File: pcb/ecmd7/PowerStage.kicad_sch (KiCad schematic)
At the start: 36 parts, among them Q1 IRFS3806, Q2 IRFS3806, Q3 IRFS3806, Q4 IRFS3806, Q5 IRFS3806, Q6 IRFS3806, U1 TMC6200-TA

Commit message: WIP: Add supply
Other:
- moved on the sheet: Q2, Q4, Q6, R2, R4, R7
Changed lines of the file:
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@@
 	(wire
 		(pts
+			(xy 290.83 171.45) (xy 300.99 171.45)
+		)
+		(stroke
+			(width 0)
+			(type default)
+		)
+	)
+	(wire
+		(pts
 			(xy 137.16 54.61) (xy 137.16 57.15)
 		)
@@
 	(wire
 		(pts
-			(xy 308.61 72.39) (xy 308.61 76.2)
+			(xy 308.61 73.66) (xy 308.61 76.2)
 		)
 		(stroke
@@
 	(wire
 		(pts
-			(xy 308.61 113.03) (xy 308.61 114.3)
+			(xy 308.61 113.03) (xy 308.61 115.57)
 		)
 		(stroke
@@
 	(wire
 		(pts
-			(xy 251.46 170.18) (xy 283.21 170.18)
+			(xy 251.46 171.45) (xy 283.21 171.45)
 		)
 		(stroke
@@
 	(wire
 		(pts
-			(xy 290.83 67.31) (xy 300.99 67.31)
+			(xy 290.83 68.58) (xy 300.99 68.58)
 		)
 		(stroke
@@
 	(wire
 		(pts
-			(xy 256.54 67.31) (xy 283.21 67.31)
+			(xy 256.54 68.58) (xy 283.21 68.58)
 		)
 		(stroke
@@
 	(wire
 		(pts
+			(xy 290.83 120.65) (xy 300.99 120.65)
+		)
+		(stroke
+			(width 0)
+			(type default)
+		)
+	)
+	(wire
+		(pts
 			(xy 256.54 163.83) (xy 308.61 163.83)
 		)
@@
 	(wire
 		(pts
-			(xy 256.54 67.31) (xy 256.54 102.87)
+			(xy 256.54 68.58) (xy 256.54 102.87)
 		)
 		(stroke
@@
 	(wire
 		(pts
-			(xy 251.46 133.35) (xy 251.46 170.18)
+			(xy 251.46 133.35) (xy 251.46 171.45)
 		)
 		(stroke
@@
 	(wire
 		(pts
-			(xy 290.83 119.38) (xy 300.99 119.38)
+			(xy 308.61 125.73) (xy 308.61 128.27)
 		)
 		(stroke
@@
 	(wire
 		(pts
-			(xy 308.61 124.46) (xy 308.61 128.27)
-		)
-		(stroke
-			(width 0)
-			(type default)
-		)
-	)
-	(wire
-		(pts
-			(xy 308.61 163.83) (xy 308.61 165.1)
+			(xy 308.61 163.83) (xy 308.61 166.37)
 		)
 		(stroke
@@
 	(wire
 		(pts
-			(xy 290.83 170.18) (xy 300.99 170.18)
-		)
-		(stroke
-			(width 0)
-			(type default)
-		)
-	)
-	(wire
-		(pts
 			(xy 219.71 92.71) (xy 237.49 92.71)
 		)
@@
 	(wire
 		(pts
-			(xy 265.43 119.38) (xy 265.43 118.11)
+			(xy 265.43 120.65) (xy 265.43 118.11)
 		)
 		(stroke
@@
 	(wire
 		(pts
-			(xy 265.43 119.38) (xy 283.21 119.38)
+			(xy 265.43 120.65) (xy 283.21 120.65)
 		)
 		(stroke
@@
 	(wire
 		(pts
-			(xy 308.61 175.26) (xy 308.61 179.07)
+			(xy 308.61 176.53) (xy 308.61 179.07)
 		)
 		(stroke
@@
 	(wire
 		(pts
-			(xy 308.61 60.96) (xy 308.61 62.23)
+			(xy 308.61 60.96) (xy 308.61 63.5)
 		)
 		(stroke
@@
 	(symbol
 		(lib_id "Device:R")
-		(at 287.02 67.31 90)
+		(at 287.02 68.58 90)
 		(unit 1)
 		(exclude_from_sim no)
@@
 		(dnp no)
 		(property "Reference" "R2"
-			(at 285.496 65.024 90)
+			(at 285.496 66.294 90)
 			(effects
 				(font
@@
 		)
 		(property "Value" "0.47"
-			(at 286.512 69.596 90)
+			(at 286.512 70.866 90)
 			(effects
 				(font
@@
 		)
 		(property "Footprint" "Resistor_SMD:R_0805_2012Metric"
-			(at 287.02 69.088 90)
+			(at 287.02 70.358 90)
 			(effects
 				(font
@@
 		)
 		(property "Datasheet" "~"
-			(at 287.02 67.31 0)
+			(at 287.02 68.58 0)
 			(effects
 				(font
@@
 		)
 		(property "Description" "Resistor"
-			(at 287.02 67.31 0)
+			(at 287.02 68.58 0)
 			(effects
 				(font
@@
 	(symbol
 		(lib_id "Transistor_FET:IRFS4115")
-		(at 306.07 67.31 0)
+		(at 306.07 68.58 0)
 		(unit 1)
 		(exclude_from_sim no)
@@
 		(fields_autoplaced yes)
 		(property "Reference" "Q2"
-			(at 312.42 66.0399 0)
+			(at 312.42 67.3099 0)
 			(effects
 				(font
@@
 		)
 		(property "Value" "IRFS3806"
-			(at 312.42 68.5799 0)
+			(at 312.42 69.8499 0)
 			(effects
 				(font
@@
 		)
 		(property "Footprint" "Package_TO_SOT_SMD:TO-263-2"
-			(at 311.15 69.215 0)
+			(at 311.15 70.485 0)
 			(effects
 				(font
@@
 		)
 		(property "Datasheet" "https://www.infineon.com/assets/row/public/documents/24/49/infineon-irfs3806-datasheet-en.pdf"
-			(at 311.15 71.12 0)
+			(at 311.15 72.39 0)
 			(effects
 				(font
@@
 		)
 		(property "Description" "43A Id, 60V Vds, 12.6mOhm Rds, N-Channel HEXFET Power MOSFET, D2PAK"
-			(at 306.07 67.31 0)
+			(at 306.07 68.58 0)
 			(effects
 				(font
@@
 	(symbol
 		(lib_id "Device:R")
-		(at 287.02 170.18 90)
+		(at 287.02 171.45 90)
 		(unit 1)
 		(exclude_from_sim no)
@@
 		(dnp no)
 		(property "Reference" "R7"
-			(at 285.496 167.894 90)
+			(at 285.496 169.164 90)
 			(effects
 				(font
@@
 		)
 		(property "Value" "0.47"
-			(at 286.512 172.466 90)
+			(at 286.512 173.736 90)
 			(effects
 				(font
@@
 		)
 		(property "Footprint" "Resistor_SMD:R_0805_2012Metric"
-			(at 287.02 171.958 90)
+			(at 287.02 173.228 90)
 			(effects
 				(font
@@
 		)
 		(property "Datasheet" "~"
-			(at 287.02 170.18 0)
+			(at 287.02 171.45 0)
 			(effects
 				(font
@@
 		)
 		(property "Description" "Resistor"
-			(at 287.02 170.18 0)
+			(at 287.02 171.45 0)
 			(effects
 				(font
@@
 	(symbol
 		(lib_id "Transistor_FET:IRFS4115")
-		(at 306.07 170.18 0)
+		(at 306.07 171.45 0)
 		(unit 1)
 		(exclude_from_sim no)
@@
 		(fields_autoplaced yes)
 		(property "Reference" "Q6"
-			(at 312.42 168.9099 0)
+			(at 312.42 170.1799 0)
 			(effects
 				(font
@@
 		)
 		(property "Value" "IRFS3806"
-			(at 312.42 171.4499 0)
+			(at 312.42 172.7199 0)
 			(effects
 				(font
@@
 		)
 		(property "Footprint" "Package_TO_SOT_SMD:TO-263-2"
-			(at 311.15 172.085 0)
+			(at 311.15 173.355 0)
 			(effects
 				(font
@@
 		)
 		(property "Datasheet" "https://www.infineon.com/assets/row/public/documents/24/49/infineon-irfs3806-datasheet-en.pdf"
-			(at 311.15 173.99 0)
+			(at 311.15 175.26 0)
 			(effects
 				(font
@@
 		)
 		(property "Description" "43A Id, 60V Vds, 12.6mOhm Rds, N-Channel HEXFET Power MOSFET, D2PAK"
-			(at 306.07 170.18 0)
+			(at 306.07 171.45 0)
 			(effects
 				(font
@@
 	(symbol
 		(lib_id "Transistor_FET:IRFS4115")
-		(at 306.07 119.38 0)
+		(at 306.07 120.65 0)
 		(unit 1)
 		(exclude_from_sim no)
@@
 		(fields_autoplaced yes)
 		(property "Reference" "Q4"
-			(at 312.42 118.1099 0)
+			(at 312.42 119.3799 0)
 			(effects
 				(font
@@
 		)
 		(property "Value" "IRFS3806"
-			(at 312.42 120.6499 0)
+			(at 312.42 121.9199 0)
 			(effects
 				(font
@@
 		)
 		(property "Footprint" "Package_TO_SOT_SMD:TO-263-2"
-			(at 311.15 121.285 0)
+			(at 311.15 122.555 0)
 			(effects
 				(font
@@
 		)
 		(property "Datasheet" "https://www.infineon.com/assets/row/public/documents/24/49/infineon-irfs3806-datasheet-en.pdf"
-			(at 311.15 123.19 0)
+			(at 311.15 124.46 0)
 			(effects
 				(font
@@
 		)
 		(property "Description" "43A Id, 60V Vds, 12.6mOhm Rds, N-Channel HEXFET Power MOSFET, D2PAK"
-			(at 306.07 119.38 0)
+			(at 306.07 120.65 0)
 			(effects
 				(font
@@
 	(symbol
 		(lib_id "Device:R")
-		(at 287.02 119.38 90)
+		(at 287.02 120.65 90)
 		(unit 1)
 		(exclude_from_sim no)
@@
 		(dnp no)
 		(property "Reference" "R4"
-			(at 285.496 117.094 90)
+			(at 285.496 118.364 90)
 			(effects
 				(font
@@
 		)
 		(property "Value" "0.47"
-			(at 286.512 121.666 90)
+			(at 286.512 122.936 90)
 			(effects
 				(font
@@
 		)
 		(property "Footprint" "Resistor_SMD:R_0805_2012Metric"
-			(at 287.02 121.158 90)
+			(at 287.02 122.428 90)
 			(effects
 				(font
@@
 		)
 		(property "Datasheet" "~"
-			(at 287.02 119.38 0)
+			(at 287.02 120.65 0)
 			(effects
 				(font
@@
 		)
 		(property "Description" "Resistor"
-			(at 287.02 119.38 0)
+			(at 287.02 120.65 0)
 			(effects
 				(font

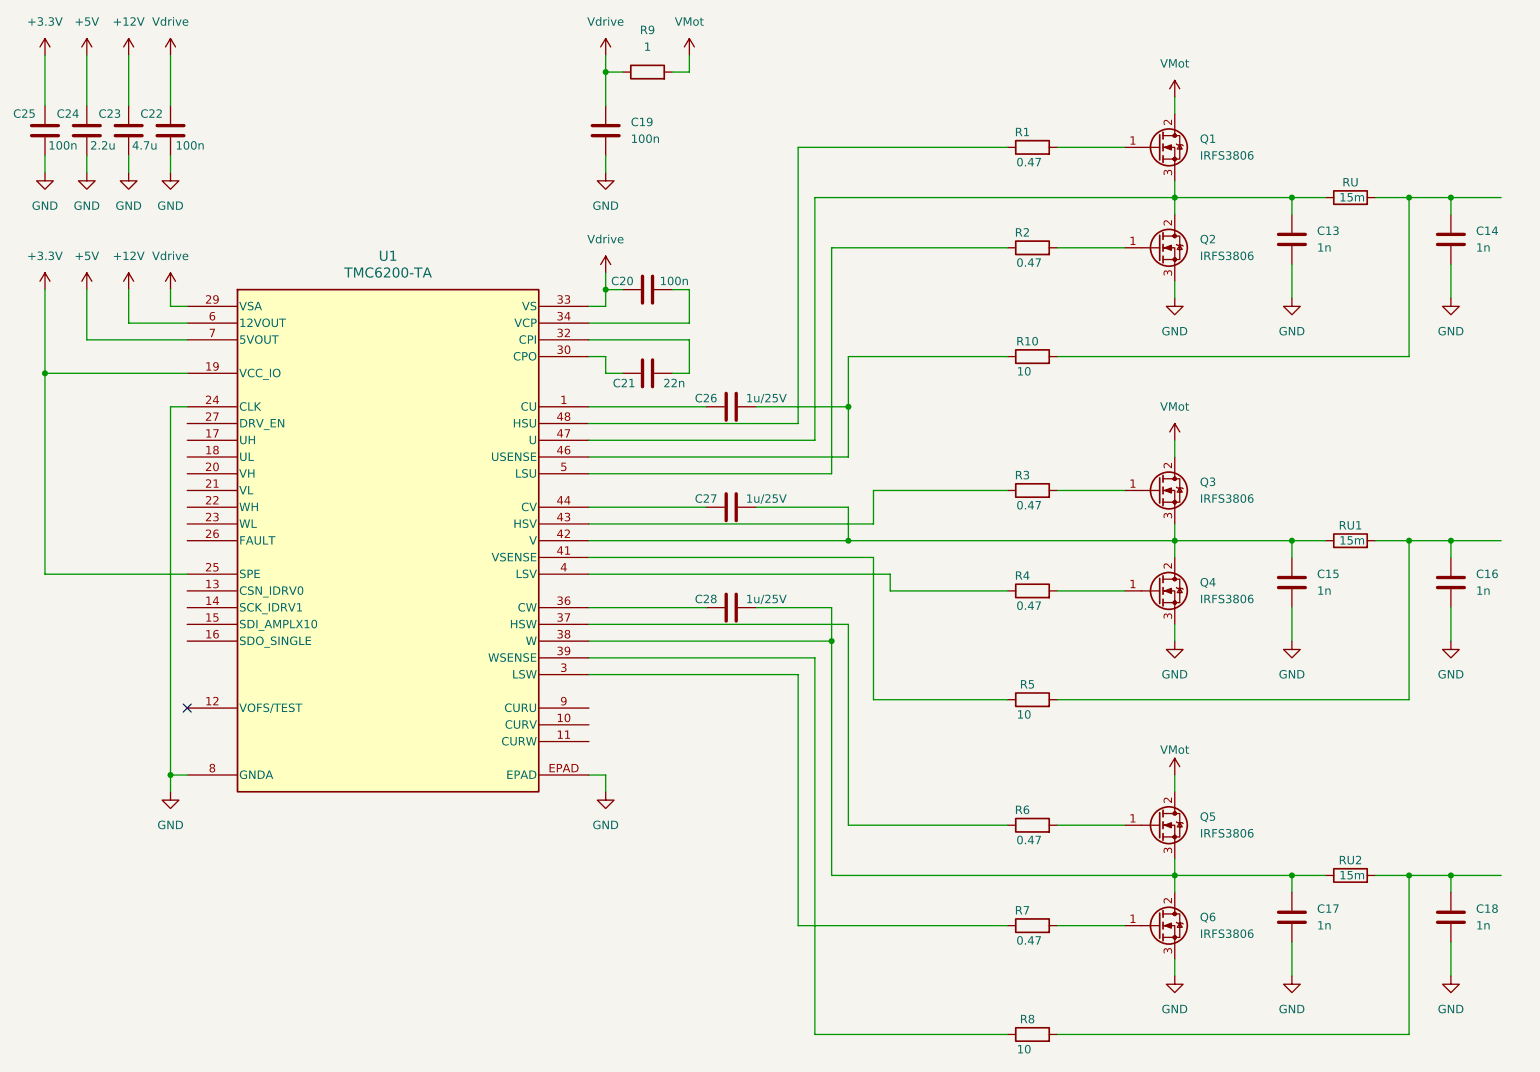
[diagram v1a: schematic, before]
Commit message: WIP: Add ADC inputs
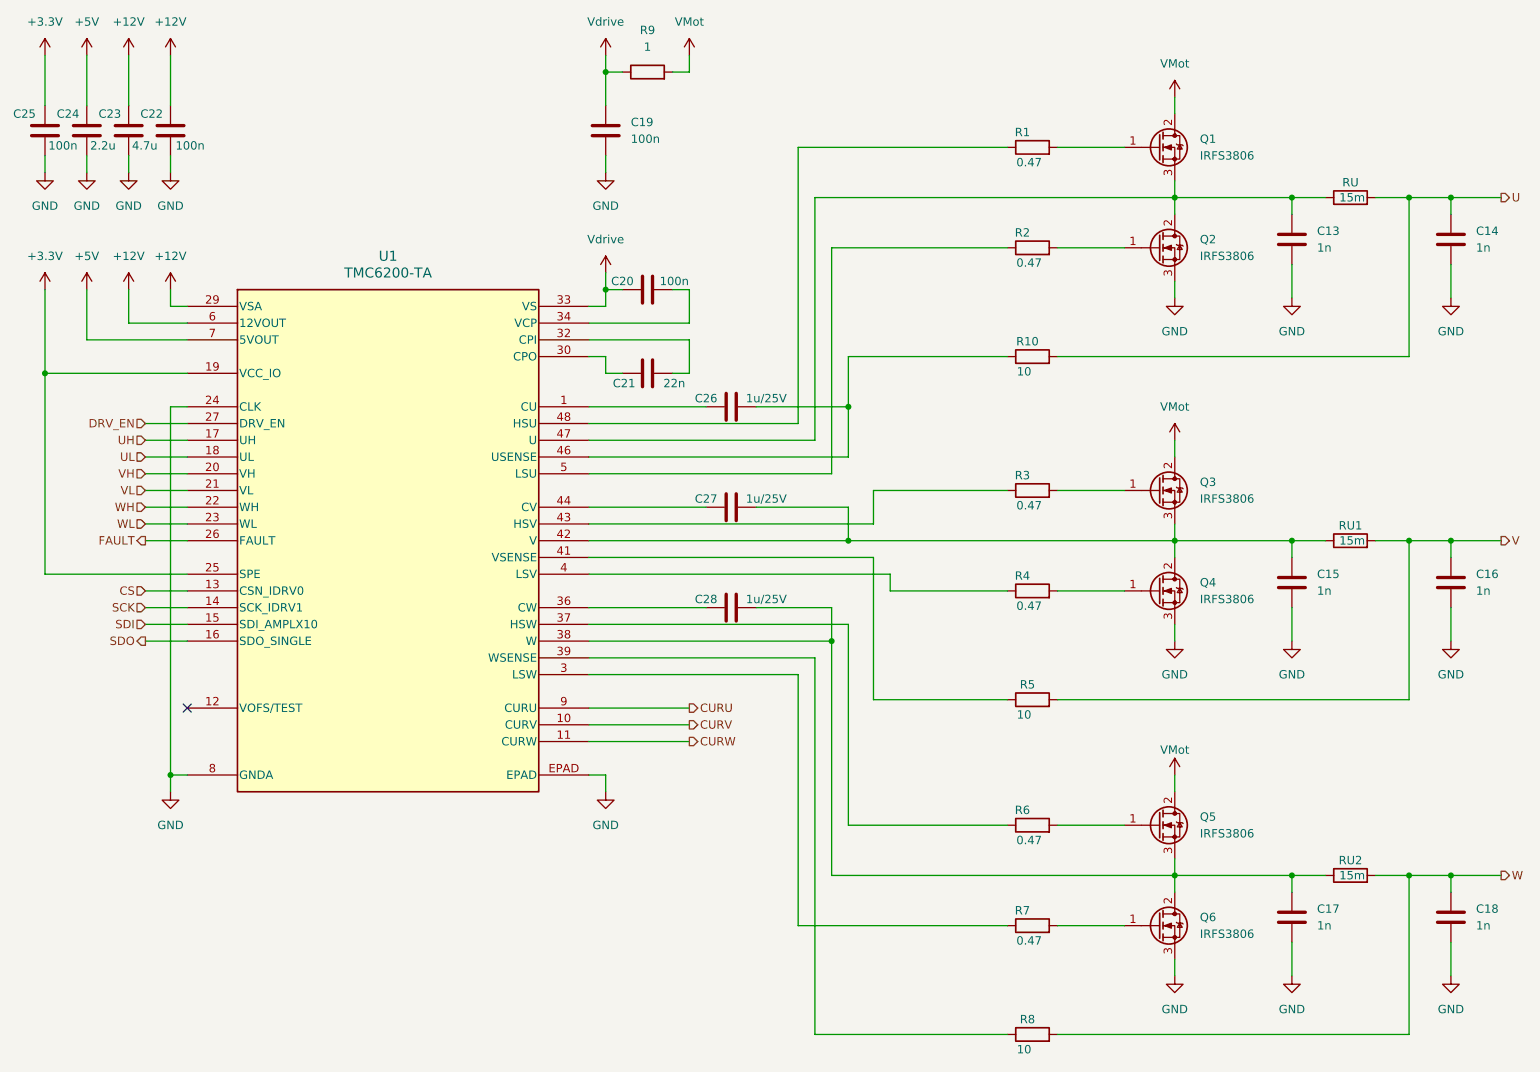
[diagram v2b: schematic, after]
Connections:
- net +12V: now also C22.1, U1.29 (VSA)
- net Vdrive: no longer C22.1, U1.29 (VSA)
- net W: now reaches C18.1, R8.2, RU2.2
- net V: now reaches C16.1, R5.2, RU1.2
- net U: now reaches C14.1, R10.2, RU.2
- net CURV: now reaches U1.10 (CURV)
- net CURW: now reaches U1.11 (CURW)
- net CS: now reaches U1.13 (CSN_IDRV0)
- net SCK: now reaches U1.14 (SCK_IDRV1)
- net SDI: now reaches U1.15 (SDI_AMPLX10)
- net SDO: now reaches U1.16 (SDO_SINGLE)
- net UH: now reaches U1.17 (UH)
- net UL: now reaches U1.18 (UL)
- net VH: now reaches U1.20 (VH)
- net VL: now reaches U1.21 (VL)
- net WH: now reaches U1.22 (WH)
- net WL: now reaches U1.23 (WL)
- net FAULT: now reaches U1.26 (FAULT)
- net DRV_EN: now reaches U1.27 (DRV_EN)
- net CURU: now reaches U1.9 (CURU)
